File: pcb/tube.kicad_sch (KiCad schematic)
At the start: 82 parts, among them J1 Screw_Terminal_01x02, J10 LED_[5..8], J11 LED_[1..4], J2 Screw_Terminal_01x02, J3 Screw_Terminal_01x02, J4 Conn_01x04_Pin, J5 Conn_01x10_Pin, J6 Conn_01x05_Pin, U1 INA226, U10 74LS32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

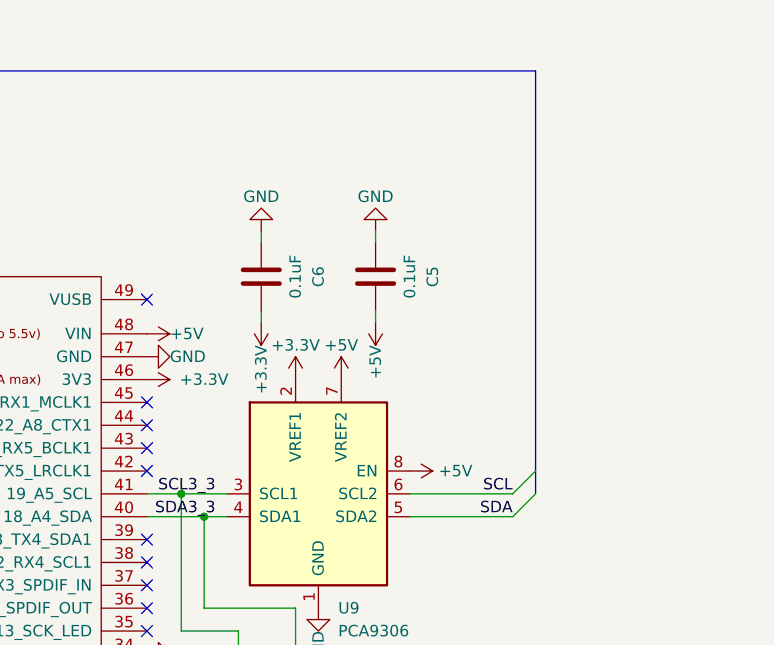
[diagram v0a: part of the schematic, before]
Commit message: PCB: Fulfill PCA9306 Spec
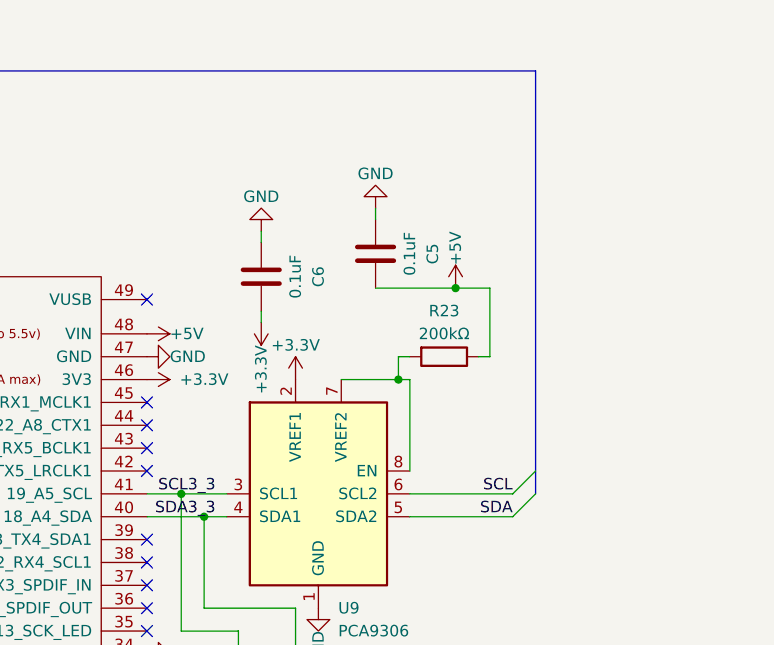
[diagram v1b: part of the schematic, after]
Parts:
- added R23: 200kΩ, Resistor_SMD:R_0805_2012Metric, symbol Device:R
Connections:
- net +5V: now also R23.1; no longer U9.7 (VREF2), U9.8 (EN)
- new net: R23.2, U9.7 (VREF2), U9.8 (EN)
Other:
- moved on the sheet: C5
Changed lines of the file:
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@@
   (junction (at 170.18 22.86) (diameter 0) (color 0 0 0 0)
   )
+  (junction (at 298.45 62.23) (diameter 0) (color 0 0 0 0)
+  )
   (junction (at 19.05 205.74) (diameter 0) (color 0 0 0 0)
   )
@@
   (junction (at 25.4 92.71) (diameter 0) (color 0 0 0 0)
   )
+  (junction (at 292.1 72.39) (diameter 0) (color 0 0 0 0)
+  )
   (junction (at 34.29 45.72) (diameter 0) (color 0 0 0 0)
   )
@@
     (stroke (width 0) (type default))
   )
+  (wire (pts (xy 302.26 69.85) (xy 302.26 62.23))
+    (stroke (width 0) (type default))
+  )
   (bus (pts (xy 149.86 76.2) (xy 149.86 78.74))
     (stroke (width 0) (type default))
@@
     (stroke (width 0) (type default))
   )
+  (wire (pts (xy 292.1 72.39) (xy 292.1 69.85))
+    (stroke (width 0) (type default))
+  )
   (wire (pts (xy 46.99 81.28) (xy 44.45 81.28))
     (stroke (width 0) (type default))
@@
     (stroke (width 0) (type default))
   )
+  (wire (pts (xy 292.1 72.39) (xy 285.75 72.39))
+    (stroke (width 0) (type default))
+  )
   (wire (pts (xy 198.12 90.17) (xy 208.28 90.17))
     (stroke (width 0) (type default))
@@
     (stroke (width 0) (type default))
   )
-  (wire (pts (xy 289.56 66.04) (xy 289.56 64.77))
-    (stroke (width 0) (type default))
-  )
   (wire (pts (xy 172.72 40.64) (xy 172.72 43.18))
     (stroke (width 0) (type default))
@@
     (stroke (width 0) (type default))
   )
+  (wire (pts (xy 302.26 62.23) (xy 298.45 62.23))
+    (stroke (width 0) (type default))
+  )
   (wire (pts (xy 91.44 78.74) (xy 90.17 78.74))
     (stroke (width 0) (type default))
@@
     (stroke (width 0) (type default))
   )
+  (wire (pts (xy 293.37 82.55) (xy 293.37 72.39))
+    (stroke (width 0) (type default))
+  )
   (bus (pts (xy 274.32 189.23) (xy 274.32 191.77))
     (stroke (width 0) (type default))
@@
     (stroke (width 0) (type default))
   )
+  (wire (pts (xy 302.26 69.85) (xy 300.99 69.85))
+    (stroke (width 0) (type default))
+  )
   (wire (pts (xy 264.16 113.03) (xy 269.24 113.03))
     (stroke (width 0) (type default))
@@
     (stroke (width 0) (type default))
   )
+  (wire (pts (xy 293.37 72.39) (xy 292.1 72.39))
+    (stroke (width 0) (type default))
+  )
   (wire (pts (xy 134.62 83.82) (xy 133.35 83.82))
     (stroke (width 0) (type default))
@@
     (stroke (width 0) (type default))
   )
-  (wire (pts (xy 289.56 55.88) (xy 289.56 57.15))
+  (wire (pts (xy 289.56 53.34) (xy 289.56 54.61))
     (stroke (width 0) (type default))
   )
@@
     (stroke (width 0) (type default))
   )
+  (wire (pts (xy 298.45 62.23) (xy 289.56 62.23))
+    (stroke (width 0) (type default))
+  )
   (wire (pts (xy 91.44 81.28) (xy 90.17 81.28))
     (stroke (width 0) (type default))
@@
     (stroke (width 0) (type default))
   )
+  (wire (pts (xy 292.1 69.85) (xy 293.37 69.85))
+    (stroke (width 0) (type default))
+  )
   (wire (pts (xy 39.37 81.28) (xy 41.91 81.28))
     (stroke (width 0) (type default))
@@
     )
   )
-  (symbol (lib_id "power:GND") (at 289.56 55.88 180) (unit 1)
+  (symbol (lib_id "power:GND") (at 289.56 53.34 180) (unit 1)
     (in_bom yes) (on_board yes) (dnp no)
-    (property "Reference" "#PWR052" (at 289.56 49.53 0)
+    (property "Reference" "#PWR052" (at 289.56 46.99 0)
       (effects (font (size 1.27 1.27)) hide)
     )
-    (property "Value" "GND" (at 289.56 52.07 0)
+    (property "Value" "GND" (at 289.56 49.53 0)
       (effects (font (size 1.27 1.27)))
     )
-    (property "Footprint" "" (at 289.56 55.88 0)
+    (property "Footprint" "" (at 289.56 53.34 0)
       (effects (font (size 1.27 1.27)) hide)
     )
-    (property "Datasheet" "" (at 289.56 55.88 0)
+    (property "Datasheet" "" (at 289.56 53.34 0)
       (effects (font (size 1.27 1.27)) hide)
     )
@@
     )
   )
-  (symbol (lib_id "power:+5V") (at 293.37 82.55 270) (unit 1)
-    (in_bom yes) (on_board yes) (dnp no)
-    (property "Reference" "#PWR051" (at 289.56 82.55 0)
-      (effects (font (size 1.27 1.27)) hide)
-    )
-    (property "Value" "+5V" (at 298.45 82.55 90)
-      (effects (font (size 1.27 1.27)))
-    )
-    (property "Footprint" "" (at 293.37 82.55 0)
-      (effects (font (size 1.27 1.27)) hide)
-    )
-    (property "Datasheet" "" (at 293.37 82.55 0)
-      (effects (font (size 1.27 1.27)) hide)
-    )
-    (pin "1")
-    (instances
-      (project "tube"
-        (path "/17a681e7-f555-4501-b0f6-333651e2bfd6"
-          (reference "#PWR051") (unit 1)
-        )
-      )
-    )
-  )
   (symbol (lib_id "power:GND") (at 29.21 22.86 270) (unit 1)
     (in_bom yes) (on_board yes) (dnp no) (fields_autoplaced)
@@
     )
   )
-  (symbol (lib_id "power:+5V") (at 285.75 72.39 0) (unit 1)
-    (in_bom yes) (on_board yes) (dnp no)
-    (property "Reference" "#PWR047" (at 285.75 76.2 0)
-      (effects (font (size 1.27 1.27)) hide)
-    )
-    (property "Value" "+5V" (at 285.75 68.58 0)
-      (effects (font (size 1.27 1.27)))
-    )
-    (property "Footprint" "" (at 285.75 72.39 0)
-      (effects (font (size 1.27 1.27)) hide)
-    )
-    (property "Datasheet" "" (at 285.75 72.39 0)
-      (effects (font (size 1.27 1.27)) hide)
-    )
-    (pin "1")
-    (instances
-      (project "tube"
-        (path "/17a681e7-f555-4501-b0f6-333651e2bfd6"
-          (reference "#PWR047") (unit 1)
-        )
-      )
-    )
-  )
   (symbol (lib_id "power:GND") (at 203.2 46.99 180) (unit 1)
     (in_bom yes) (on_board yes) (dnp no)
@@
     )
   )
-  (symbol (lib_id "Device:C") (at 289.56 60.96 0) (unit 1)
+  (symbol (lib_id "Device:C") (at 289.56 58.42 0) (unit 1)
     (in_bom yes) (on_board yes) (dnp no)
-    (property "Reference" "C5" (at 295.91 60.96 90)
+    (property "Reference" "C5" (at 295.91 58.42 90)
       (effects (font (size 1.27 1.27)))
     )
-    (property "Value" "0.1uF" (at 293.37 60.96 90)
+    (property "Value" "0.1uF" (at 293.37 58.42 90)
       (effects (font (size 1.27 1.27)))
     )
-    (property "Footprint" "Capacitor_SMD:C_0805_2012Metric" (at 290.5252 64.77 0)
+    (property "Footprint" "Capacitor_SMD:C_0805_2012Metric" (at 290.5252 62.23 0)
       (effects (font (size 1.27 1.27)) hide)
     )
-    (property "Datasheet" "~" (at 289.56 60.96 0)
+    (property "Datasheet" "~" (at 289.56 58.42 0)
       (effects (font (size 1.27 1.27)) hide)
     )
@@
     )
   )
+  (symbol (lib_id "Device:R") (at 297.18 69.85 270) (unit 1)
+    (in_bom yes) (on_board yes) (dnp no)
+    (property "Reference" "R23" (at 297.18 64.77 90)
+      (effects (font (size 1.27 1.27)))
+    )
+    (property "Value" "200kΩ" (at 297.18 67.31 90)
+      (effects (font (size 1.27 1.27)))
+    )
+    (property "Footprint" "Resistor_SMD:R_0805_2012Metric" (at 297.18 68.072 90)
+      (effects (font (size 1.27 1.27)) hide)
+    )
+    (property "Datasheet" "~" (at 297.18 69.85 0)
+      (effects (font (size 1.27 1.27)) hide)
+    )
+    (pin "1")
+    (pin "2")
+    (instances
+      (project "tube"
+        (path "/17a681e7-f555-4501-b0f6-333651e2bfd6"
+          (reference "R23") (unit 1)
+        )
+      )
+    )
+  )
   (symbol (lib_id "power:GND") (at 128.27 152.4 90) (mirror x) (unit 1)
     (in_bom yes) (on_board yes) (dnp no)
@@
     )
   )
-  (symbol (lib_id "power:+5V") (at 289.56 66.04 180) (unit 1)
-    (in_bom yes) (on_board yes) (dnp no)
-    (property "Reference" "#PWR053" (at 289.56 62.23 0)
-      (effects (font (size 1.27 1.27)) hide)
-    )
-    (property "Value" "+5V" (at 289.56 68.58 90)
-      (effects (font (size 1.27 1.27)) (justify left))
-    )
-    (property "Footprint" "" (at 289.56 66.04 0)
-      (effects (font (size 1.27 1.27)) hide)
-    )
-    (property "Datasheet" "" (at 289.56 66.04 0)
-      (effects (font (size 1.27 1.27)) hide)
-    )
-    (pin "1")
-    (instances
-      (project "tube"
-        (path "/17a681e7-f555-4501-b0f6-333651e2bfd6"
-          (reference "#PWR053") (unit 1)
-        )
-      )
-    )
-  )
   (symbol (lib_id "Device:C") (at 276.86 60.96 0) (unit 1)
     (in_bom yes) (on_board yes) (dnp no)
@@
         )
       )
+    )
+  )
+  (symbol (lib_id "power:+5V") (at 298.45 62.23 0) (mirror y) (unit 1)
+    (in_bom yes) (on_board yes) (dnp no)
+    (property "Reference" "#PWR047" (at 298.45 66.04 0)
+      (effects (font (size 1.27 1.27)) hide)
+    )
+    (property "Value" "+5V" (at 298.45 59.69 90)
+      (effects (font (size 1.27 1.27)) (justify left))
+    )
+    (property "Footprint" "" (at 298.45 62.23 0)
+      (effects (font (size 1.27 1.27)) hide)
+    )
+    (property "Datasheet" "" (at 298.45 62.23 0)
+      (effects (font (size 1.27 1.27)) hide)
+    )
+    (pin "1")
+    (instances
+      (project "tube"
+        (path "/17a681e7-f555-4501-b0f6-333651e2bfd6"
+          (reference "#PWR047") (unit 1)
+        )
+      )

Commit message: PCB: Change Optocoupler Resistor Values
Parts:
- R20, R24: value 330Ω -> 360Ω
- R21: value 330Ω -> 170Ω
- R25: value 330Ω -> 1kΩ
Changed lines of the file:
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@@
       (effects (font (size 1.27 1.27)) (justify bottom))
     )
-    (property "Value" "330Ω" (at 214.63 204.47 90)
+    (property "Value" "1kΩ" (at 214.63 204.47 90)
       (effects (font (size 1.27 1.27)) (justify bottom))
     )
@@
       (effects (font (size 1.27 1.27)) (justify bottom))
     )
-    (property "Value" "330Ω" (at 240.03 187.96 90)
+    (property "Value" "170Ω" (at 240.03 187.96 90)
       (effects (font (size 1.27 1.27)) (justify bottom))
     )
@@
       (effects (font (size 1.27 1.27)) (justify bottom))
     )
-    (property "Value" "330Ω" (at 214.63 187.96 90)
+    (property "Value" "360Ω" (at 214.63 187.96 90)
       (effects (font (size 1.27 1.27)) (justify bottom))
     )
@@
       (effects (font (size 1.27 1.27)) (justify bottom))
     )
-    (property "Value" "330Ω" (at 240.03 204.47 90)
+    (property "Value" "360Ω" (at 240.03 204.47 90)
       (effects (font (size 1.27 1.27)) (justify bottom))
     )
